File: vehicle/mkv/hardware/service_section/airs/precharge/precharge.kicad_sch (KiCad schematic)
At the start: 4 parts

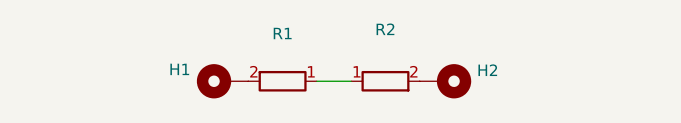
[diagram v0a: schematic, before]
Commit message: chore: annotate migrated schematics
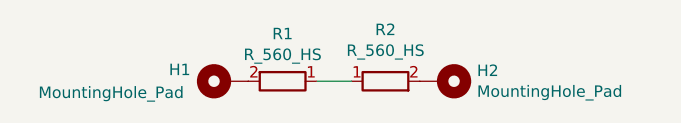
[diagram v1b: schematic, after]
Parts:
- H1, H2: value (none) -> MountingHole_Pad; footprint (none) -> MountingHole:MountingHole_2.5mm_Pad
- R1, R2: value (none) -> R_560_HS; footprint (none) -> footprints:R_3k_HS_TO247
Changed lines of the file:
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@@
     (in_bom yes) (on_board yes)
     (property "Reference" "H1" (id 0) (at 364.49 224.79 90))
-    (property "Value" "" (id 1) (at 356.87 227.33 90))
-    (property "Footprint" "" (id 2) (at 369.57 226.06 0)
+    (property "Value" "MountingHole_Pad" (id 1) (at 356.87 227.33 90))
+    (property "Footprint" "MountingHole:MountingHole_2.5mm_Pad" (id 2) (at 369.57 226.06 0)
       (effects (font (size 1.27 1.27)) hide)
     )
@@
       (effects (font (size 1.27 1.27)) (justify left))
     )
-    (property "Value" "" (id 1) (at 397.51 227.203 90)
+    (property "Value" "MountingHole_Pad" (id 1) (at 397.51 227.203 90)
       (effects (font (size 1.27 1.27)) (justify left))
     )
-    (property "Footprint" "" (id 2) (at 393.7 226.06 0)
+    (property "Footprint" "MountingHole:MountingHole_2.5mm_Pad" (id 2) (at 393.7 226.06 0)
       (effects (font (size 1.27 1.27)) hide)
     )
@@
     (in_bom yes) (on_board yes)
     (property "Reference" "R1" (id 0) (at 375.92 220.8022 90))
-    (property "Value" "" (id 1) (at 375.92 223.1136 90))
-    (property "Footprint" "" (id 2) (at 375.92 224.282 0)
+    (property "Value" "R_560_HS" (id 1) (at 375.92 223.1136 90))
+    (property "Footprint" "footprints:R_3k_HS_TO247" (id 2) (at 375.92 224.282 0)
       (effects (font (size 1.27 1.27)) hide)
     )
@@
     (in_bom yes) (on_board yes)
     (property "Reference" "R2" (id 0) (at 387.35 220.345 90))
-    (property "Value" "" (id 1) (at 387.35 222.6564 90))
-    (property "Footprint" "" (id 2) (at 387.35 227.838 0)
+    (property "Value" "R_560_HS" (id 1) (at 387.35 222.6564 90))
+    (property "Footprint" "footprints:R_3k_HS_TO247" (id 2) (at 387.35 227.838 0)
       (effects (font (size 1.27 1.27)) hide)
     )
